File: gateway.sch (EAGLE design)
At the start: 14 parts, among them J1 RASPBERRYPI-40-PIN-GPIO_PTH_N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, Q1 BSS123

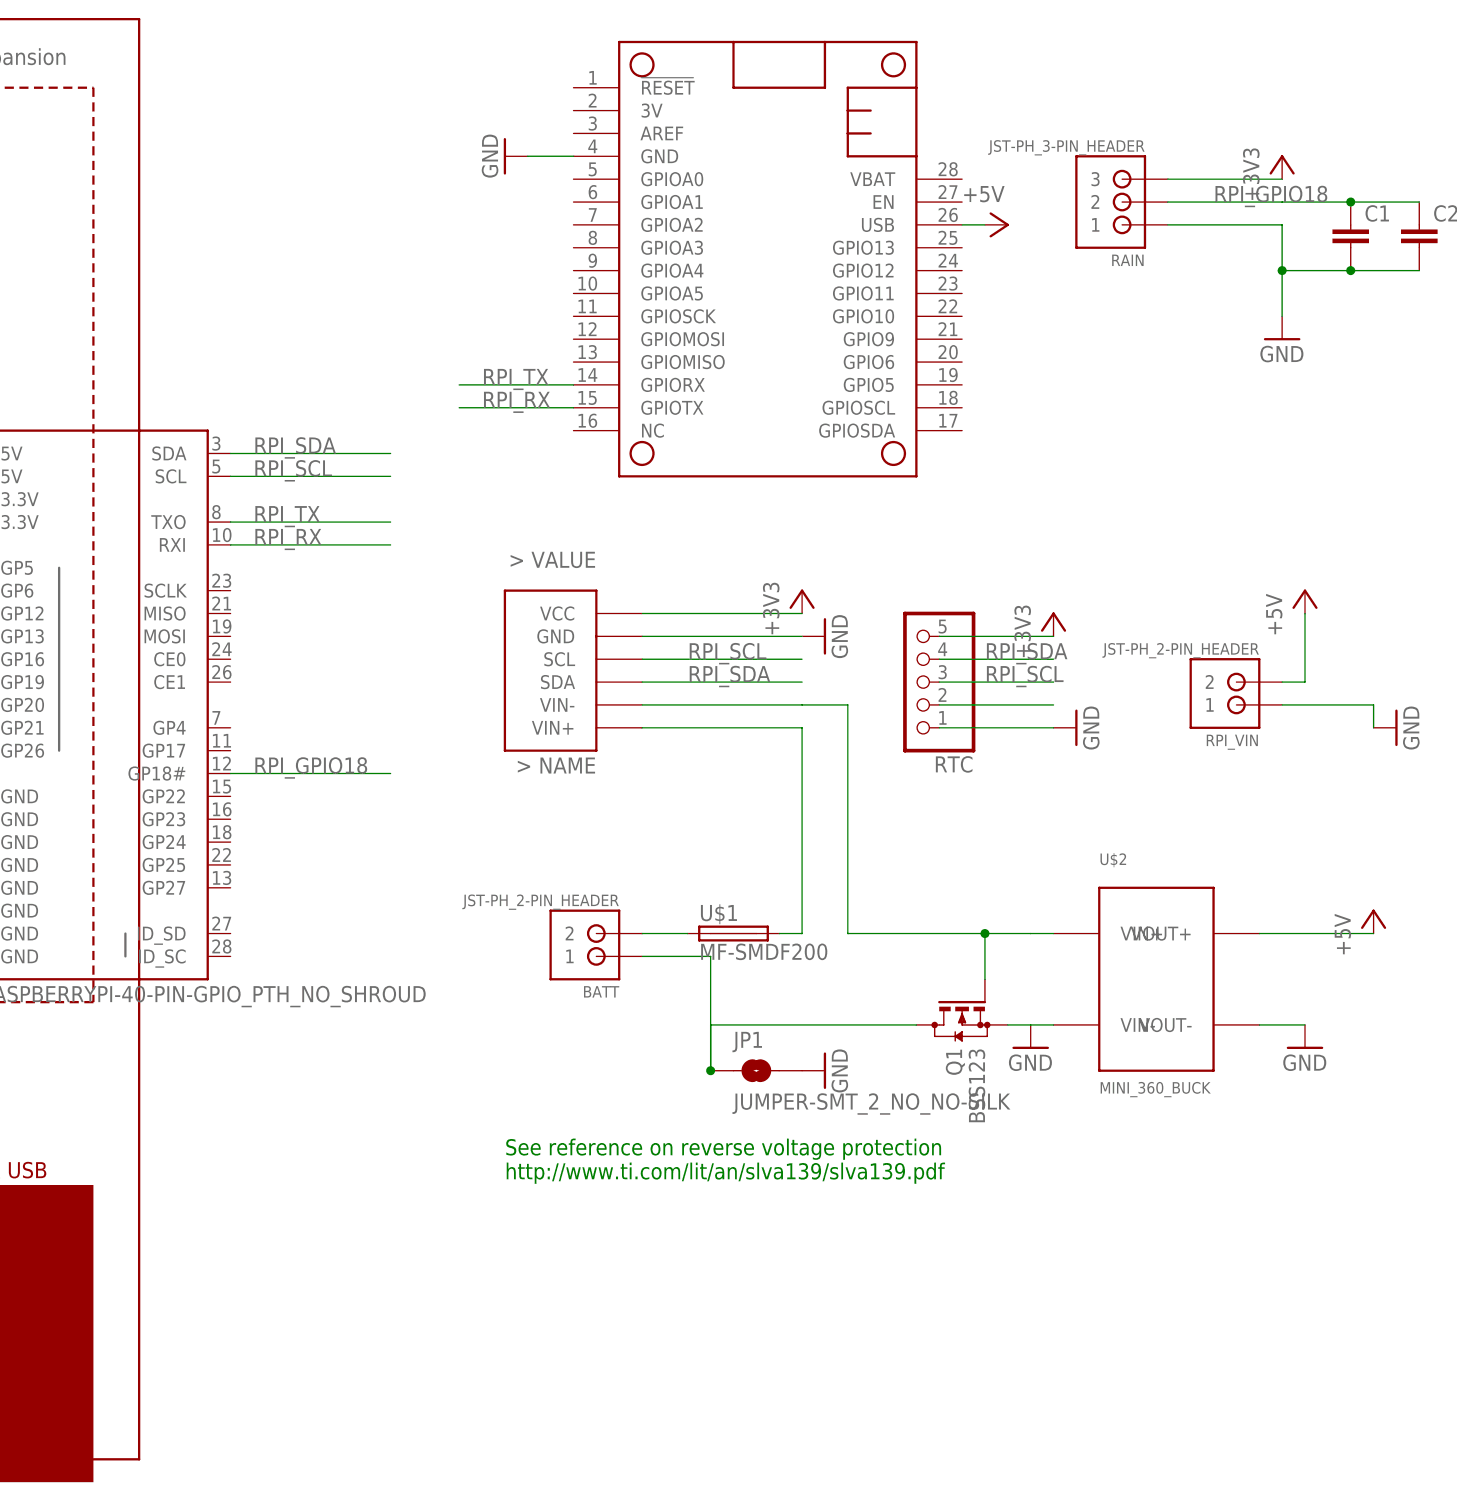
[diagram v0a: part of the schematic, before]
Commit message: added solar charge controller and delay timer. still need edits on the supply line of feather board.
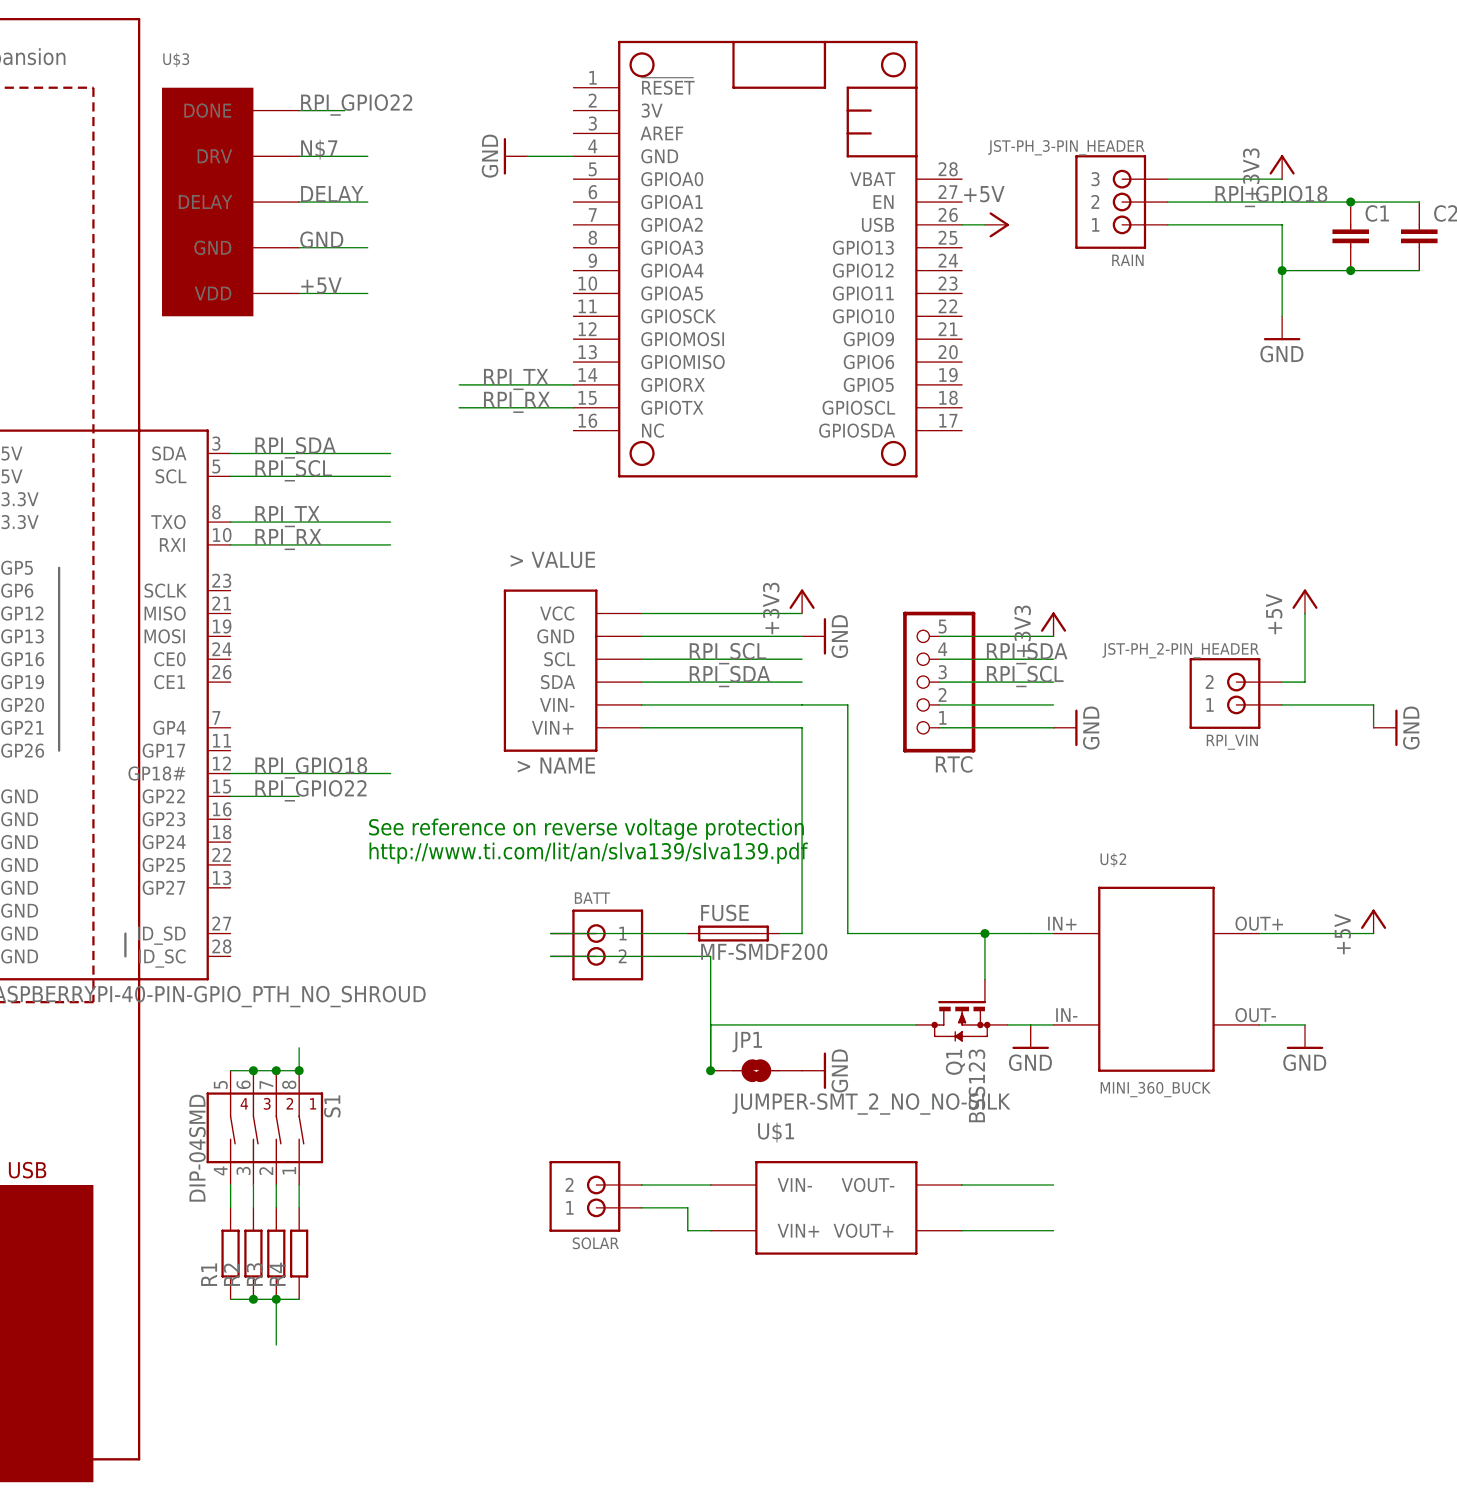
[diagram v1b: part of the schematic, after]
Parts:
- added FUSE: MF-SMDF200, fuse:MF-SMDF200
- added R1, R2, R3, R4: (no value), rcl:R-EU_0204/5
- added S1: DIP-04SMD, SparkFun-Switches:DIP-04SMD
- added SOLAR: JST-PH_2-PIN_HEADER, SRG:JST-PH_2-PIN_HEADER
- added U$3: TPL5110_BREAKOUT, edc_modules:TPL5110_BREAKOUT
- U$1: value MF-SMDF200 -> TP5100; device fuse:MF-SMDF200 -> edc_modules:TP5100
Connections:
- removed net N$2: BATT.2, U$1.1
- new net BATT+: BATT.1, FUSE.1, U$1.VOUT+
- new net BATT-: BATT.2, JP1.1, Q1.D, U$1.VOUT-
- new net DELAY: S1.1B, S1.2B, S1.3B, S1.4B, U$3.DELAY
- new net N$10: R2.2, S1.3A
- new net N$11: R3.2, S1.2A
- new net N$12: R4.2, S1.1A
- new net N$8: SOLAR.1, U$1.VIN+
- new net N$9: R1.2, S1.4A
- new net RPI_GPIO22: J1.GP22, U$3.DONE
- new net SOLAR-: SOLAR.2, U$1.VIN-
- net +5V: now also U$3.VDD
- net GND: now also R1.1, R2.1, R3.1, R4.1, U$3.GND
- net N$6: now also FUSE.2; no longer U$1.2
- net N$7: now also U$3.DRV; no longer BATT.1, JP1.1, Q1.D
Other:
- moved on the sheet: BATT, U$2
